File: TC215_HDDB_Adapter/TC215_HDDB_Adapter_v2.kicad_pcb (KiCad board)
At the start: 2 copper layers, 32 x 69 mm, 8 parts, among them J1 Conn_02x25_Odd_Even, J2 DB25_Female, J3 Conn_02x08_Odd_Even

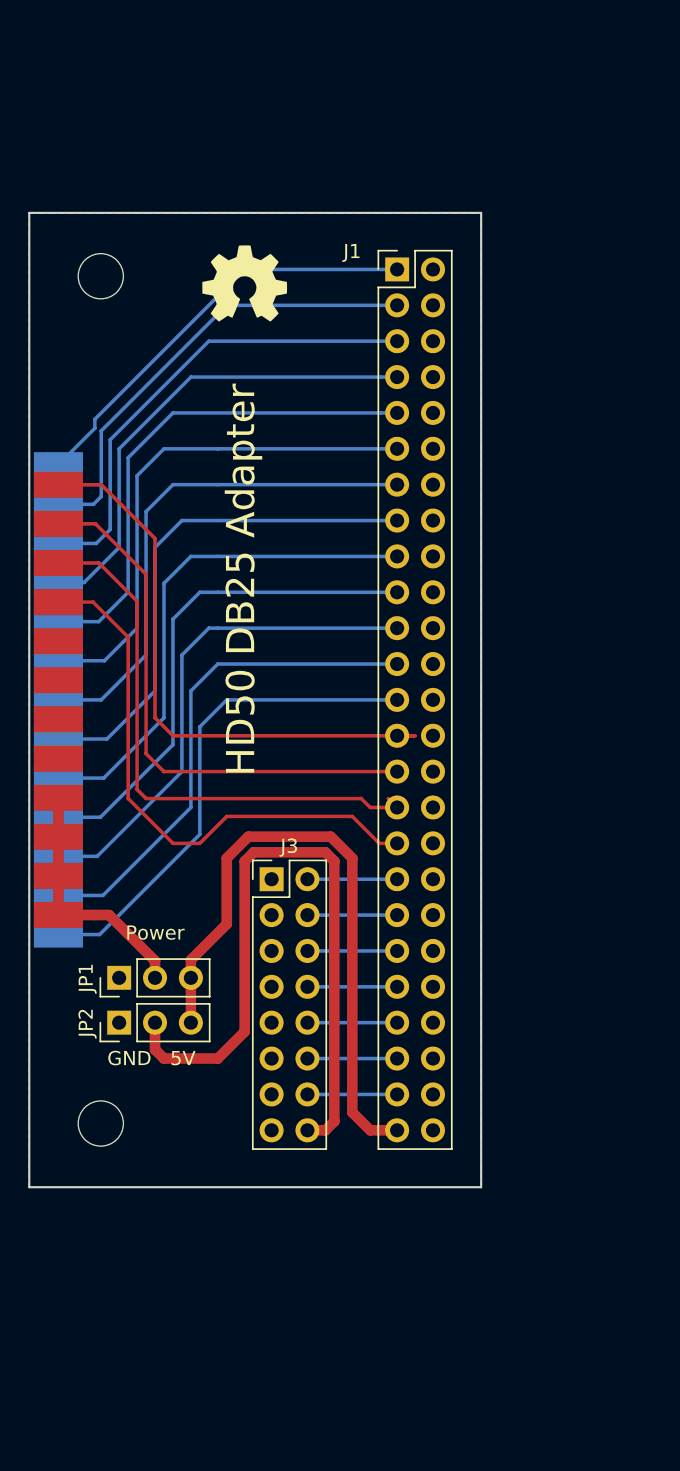
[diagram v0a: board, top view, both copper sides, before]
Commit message: new version with male DB25 connector
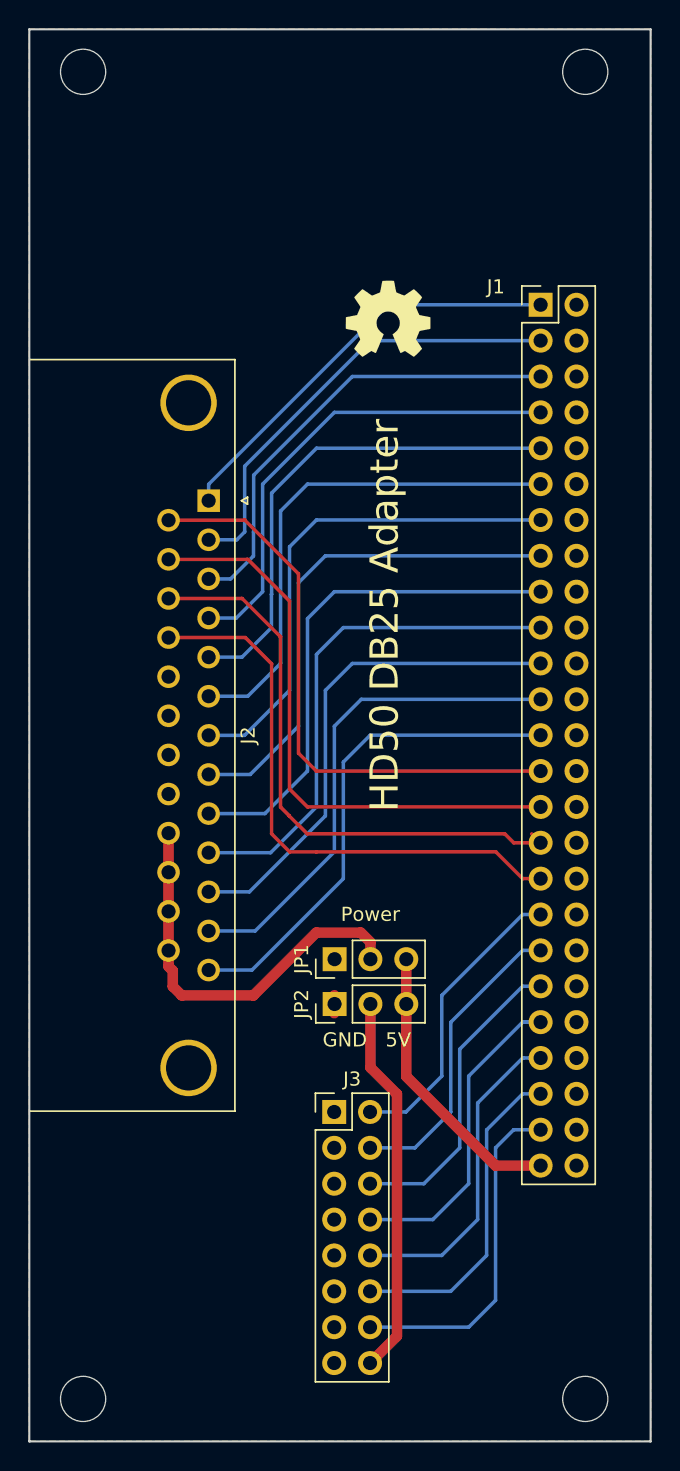
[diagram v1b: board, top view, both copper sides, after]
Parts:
- added REF**: MountingHole_3.2mm_M3_ISO7380, Mounting_Holes:MountingHole_3.2mm_M3_ISO7380, F.Cu at (114.3, 162.5)
- added REF**: MountingHole_3.2mm_M3_ISO7380, Mounting_Holes:MountingHole_3.2mm_M3_ISO7380, F.Cu at (114.3, 68.6)
- J2: value DB25_Female -> DB25_Male_MountingHoles; footprint Connectors_DSub:DSUB-25_Female_EdgeMount_Pitch2.77mm -> Connectors_DSub:DSUB-25_Male_Horizontal_Pitch2.77x2.84mm_EdgePinOffset9.90mm_Housed_MountingHolesOffset11.32mm; moved to F.Cu
- moved REF** 19.5 mm to (78.7, 162.5)
- moved J2 17.7 mm to (87.6, 98.9), turned to 270 degrees
- moved J3 17.1 mm to (96.5, 142.2)
- moved JP1 15.3 mm to (96.5, 131.4)
- moved JP2 15.3 mm to (96.5, 134.6)
- moved REF** 14.5 mm to (78.7, 68.6)
- moved G*** 10.5 mm to (100.3, 86.0)
- moved J1 10.5 mm to (111.1, 85.0)
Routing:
- net Net-(J1-Pad49): track 44.5 -> 20.4 mm
- net Net-(J3-Pad16): track 48.8 -> 27.0 mm
- net Net-(J1-Pad47): track 6.35 -> 24.2 mm
- net Net-(J1-Pad41): track 6.35 -> 23.6 mm
- net Net-(J1-Pad45): track 6.35 -> 23.1 mm
- net Net-(J1-Pad43): track 6.35 -> 22.7 mm
- net Net-(J1-Pad39): track 6.35 -> 22.0 mm
- net Net-(J1-Pad37): track 6.35 -> 21.6 mm
- net Net-(J1-Pad35): track 6.35 -> 21.2 mm
- net Net-(J2-Pad22): track 17.7 -> 28.6 mm
- net Net-(J1-Pad29): track 38.2 -> 41.4 mm
- net Net-(J1-Pad31): track 39.4 -> 41.5 mm
- net Net-(J1-Pad33): track 38.8 -> 40.5 mm
- net Net-(J1-Pad19): track 35.3 -> 36.4 mm
- net Net-(J1-Pad17): track 35.6 -> 36.3 mm
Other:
- board size 32 x 69 mm -> 44 x 100 mm
